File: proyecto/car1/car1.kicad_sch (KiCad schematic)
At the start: 20 parts, among them J1 HC-sr04, J10 Adafruit A, J2 HC-sr04, J3 HC-sr04, J4 USB_C_Receptacle_PowerOnly_6P, J5 SERVO, J6 Adafruit A, J7 Adafruit B, J8 Conn_01x19, J9 Conn_01x19, U1 TB6612FNG

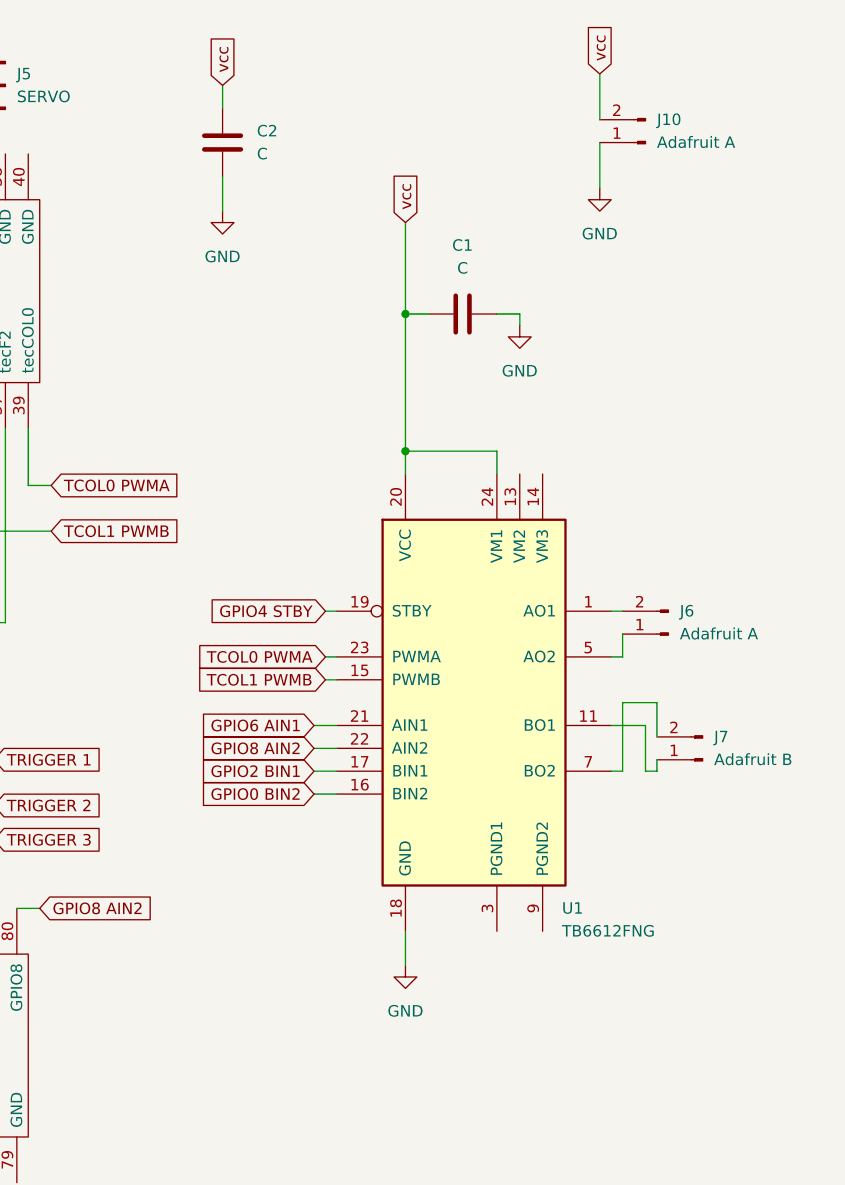
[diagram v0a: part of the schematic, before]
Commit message: se agregaron los componentes
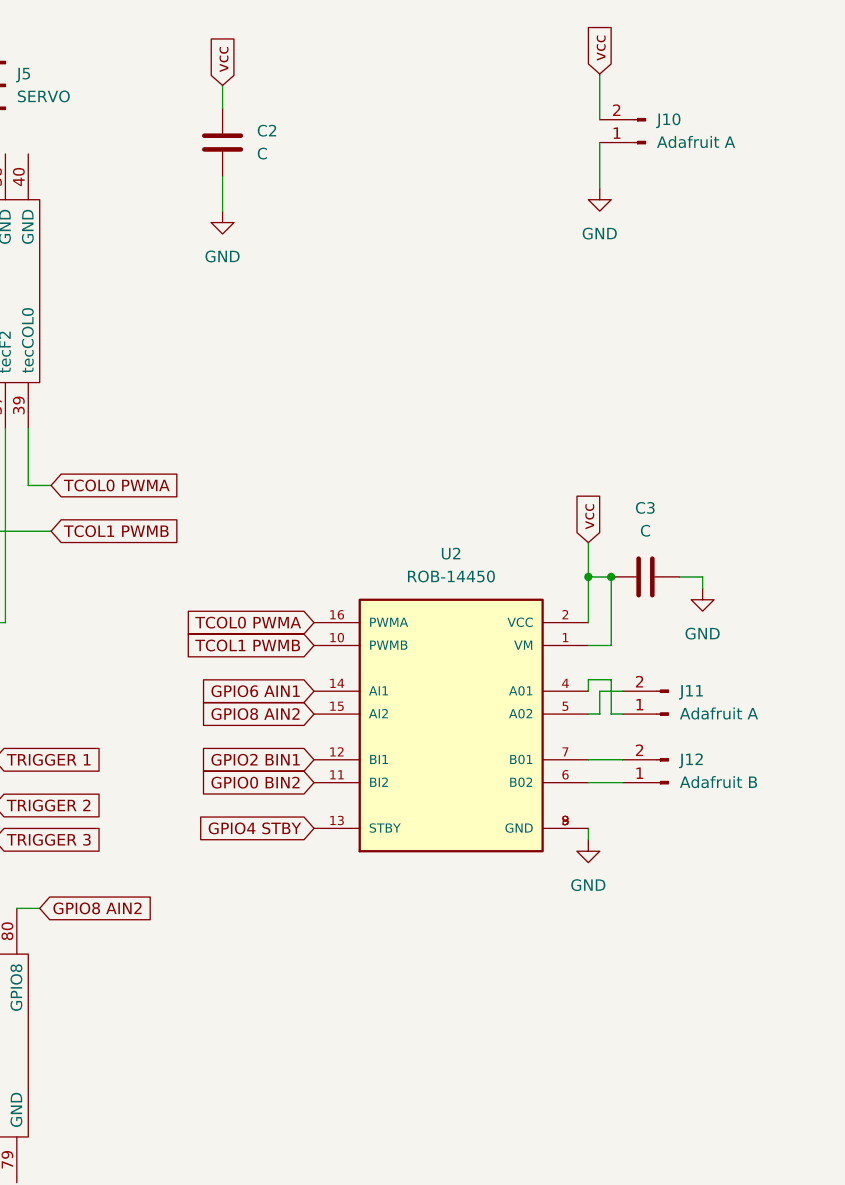
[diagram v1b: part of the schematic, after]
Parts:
- removed C1: C, Capacitor_SMD:C_0201_0603Metric, symbol Device:C
- removed J6: Adafruit A, Connector_Hirose:Hirose_DF63M-2P-3.96DSA_1x02_P3.96mm_Vertical, symbol Connector:Conn_01x02_Pin
- removed J7: Adafruit B, Connector_Hirose:Hirose_DF63M-2P-3.96DSA_1x02_P3.96mm_Vertical, symbol Connector:Conn_01x02_Pin
- removed U1: TB6612FNG, Package_SO:SSOP-24_5.3x8.2mm_P0.65mm, symbol Driver_Motor:TB6612FNG
- added C3: C, Capacitor_SMD:C_0201_0603Metric, symbol Device:C
- added J11: Adafruit A, Connector_Hirose:Hirose_DF63M-2P-3.96DSA_1x02_P3.96mm_Vertical, symbol Connector:Conn_01x02_Pin
- added J12: Adafruit B, Connector_Hirose:Hirose_DF63M-2P-3.96DSA_1x02_P3.96mm_Vertical, symbol Connector:Conn_01x02_Pin
- added U2: ROB-14450, ROB-14450:MODULE_ROB-14450, symbol ROB-14450:ROB-14450
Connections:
- net GND: now also C3.2, U2.3 (GND), U2.8 (GND), U2.9 (GND)
- net GPIO0 BIN2: now also U2.11 (BI2)
- net GPIO2 BIN1: now also U2.12 (BI1)
- net GPIO4 STBY: now also U2.13 (STBY)
- net GPIO6 AIN1: now also U2.14 (AI1)
- net GPIO8 AIN2: now also U2.15 (AI2)
- net TCOL0 PWMA: now also U2.16 (PWMA)
- net TCOL1 PWMB: now also U2.10 (PWMB)
- net vcc: now also C3.1, U2.1 (VM), U2.2 (VCC)
- new net: J11.1 (Pin_1), U2.4 (A01)
- new net: J11.2 (Pin_2), U2.5 (A02)
- new net: J12.1 (Pin_1), U2.6 (B02)
- new net: J12.2 (Pin_2), U2.7 (B01)

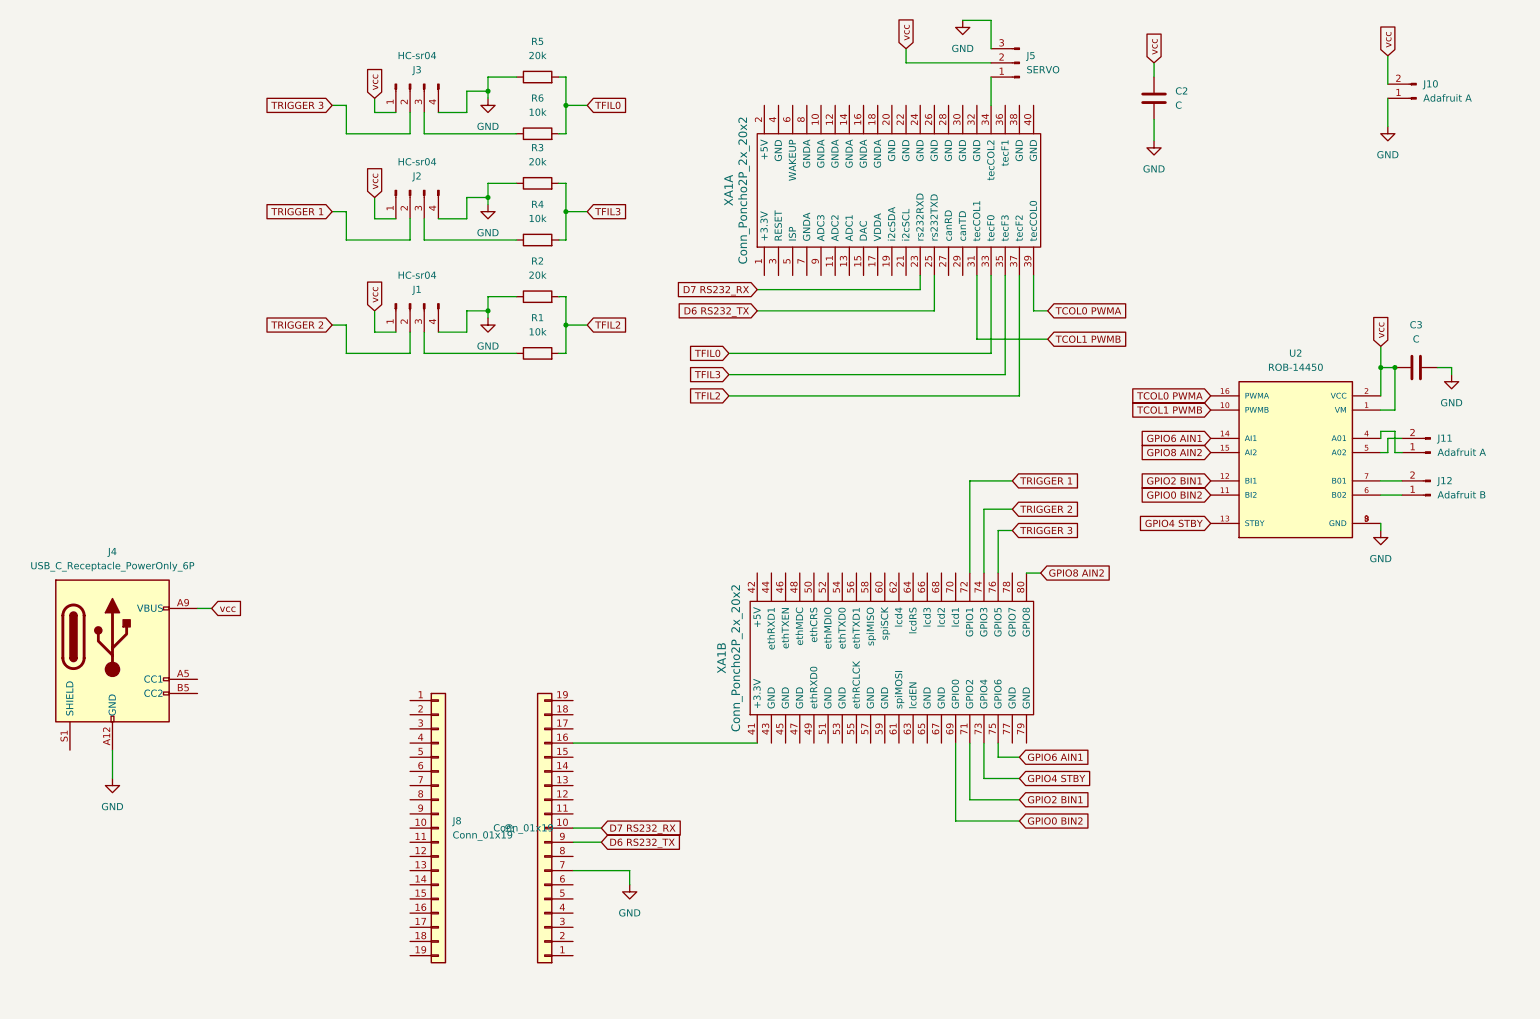
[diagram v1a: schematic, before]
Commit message: se agregaron todos los componentes
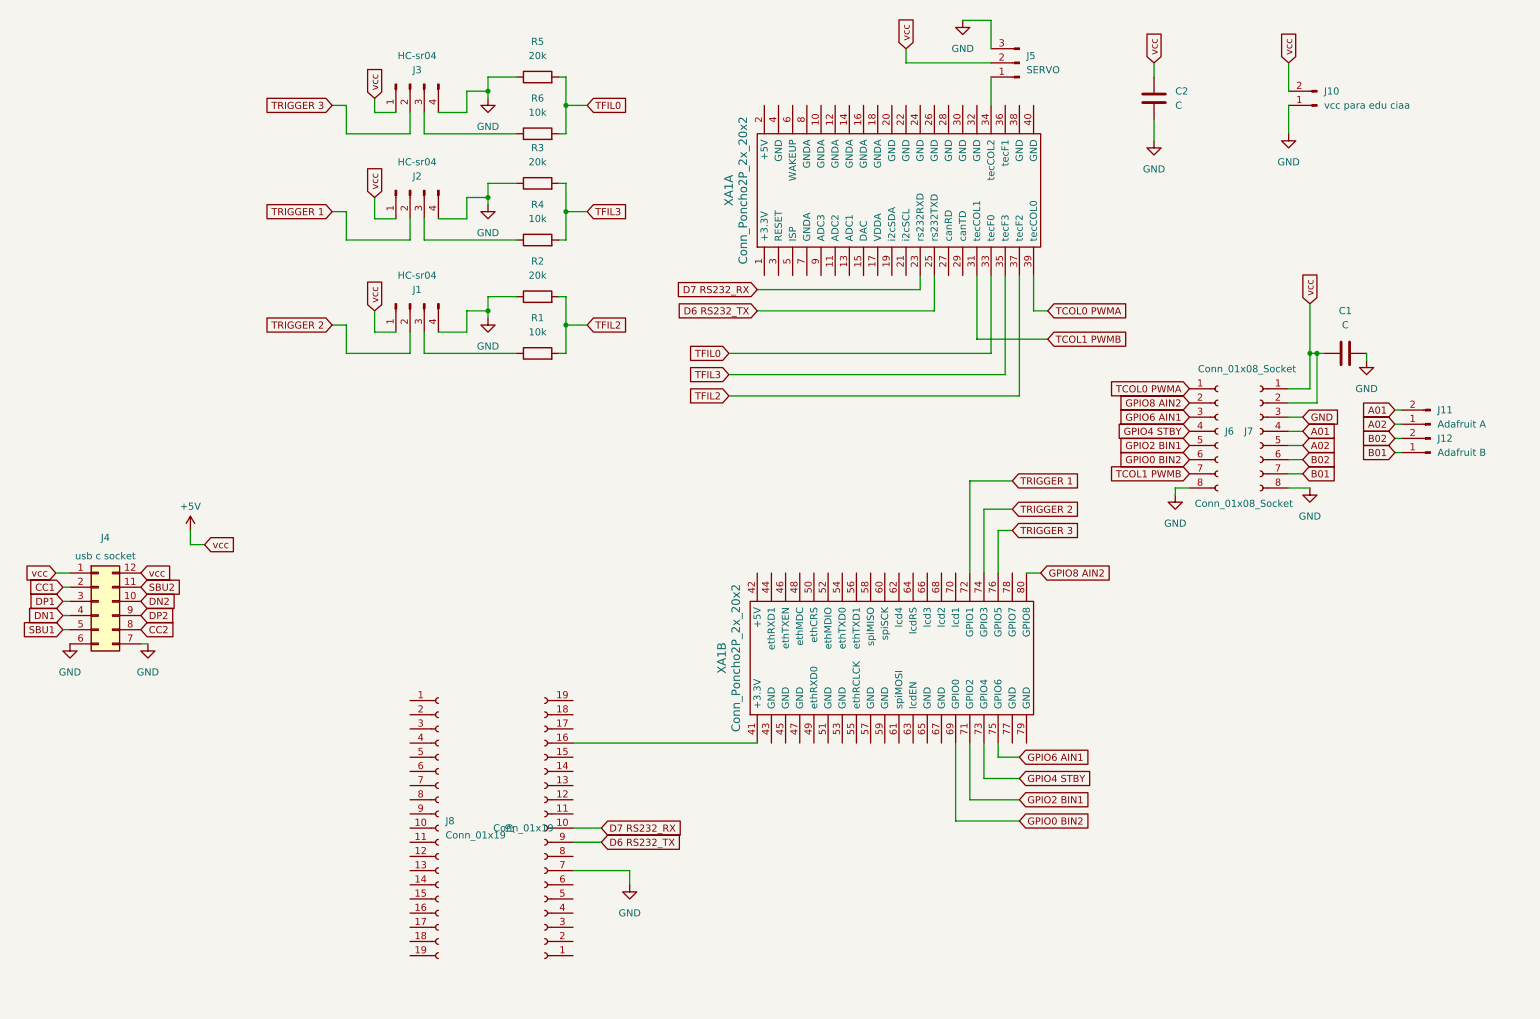
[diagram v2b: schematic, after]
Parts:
- removed C3: C, Capacitor_SMD:C_0201_0603Metric, symbol Device:C
- removed J4: USB_C_Receptacle_PowerOnly_6P, Connector_USB:USB_C_Receptacle_GCT_USB4125-xx-x-0190_6P_TopMnt_Horizontal, symbol Connector:USB_C_Receptacle_PowerOnly_6P
- removed U2: ROB-14450, ROB-14450:MODULE_ROB-14450, symbol ROB-14450:ROB-14450
- added C1: C, Capacitor_SMD:C_1206_3216Metric_Pad1.33x1.80mm_HandSolder, symbol Device:C
- added J4: usb c socket, Connector_PinSocket_2.54mm:PinSocket_2x06_P2.54mm_Vertical, symbol Connector_Generic:Conn_02x06_Counter_Clockwise
- added J6, J7: Conn_01x08_Socket, Connector_PinSocket_2.54mm:PinSocket_1x08_P2.54mm_Vertical, symbol Connector:Conn_01x08_Socket
- C2: footprint Capacitor_SMD:C_0201_0603Metric -> Capacitor_SMD:C_1206_3216Metric_Pad1.33x1.80mm_HandSolder
- J1, J2, J3: footprint Connector_Hirose:Hirose_DF63M-4P-3.96DSA_1x04_P3.96mm_Vertical -> Connector_Molex:Molex_KK-254_AE-6410-04A_1x04_P2.54mm_Vertical
- J10: value Adafruit A -> vcc para edu ciaa; footprint Connector_Hirose:Hirose_DF63M-2P-3.96DSA_1x02_P3.96mm_Vertical -> Connector_Molex:Molex_KK-254_AE-6410-02A_1x02_P2.54mm_Vertical
- J11, J12: footprint Connector_Hirose:Hirose_DF63M-2P-3.96DSA_1x02_P3.96mm_Vertical -> Connector_Molex:Molex_KK-254_AE-6410-02A_1x02_P2.54mm_Vertical
- J5: footprint Connector_JST:JST_XH_B3B-XH-A_1x03_P2.50mm_Vertical -> Connector_Molex:Molex_KK-254_AE-6410-03A_1x03_P2.54mm_Vertical
- J8, J9: footprint Connector_PinHeader_2.54mm:PinHeader_1x19_P2.54mm_Horizontal -> Connector_PinSocket_2.54mm:PinSocket_1x19_P2.54mm_Vertical; symbol Connector_Generic:Conn_01x19 -> Connector:Conn_01x19_Socket
- R1, R2, R3, R4, R5, R6: footprint Resistor_SMD:R_0201_0603Metric -> Resistor_SMD:R_1206_3216Metric_Pad1.30x1.75mm_HandSolder
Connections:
- net GND: now also C1.2, J4.6 (Pin_6), J4.7 (Pin_7), J6.8 (Pin_8), J7.3 (Pin_3), J7.8 (Pin_8)
- net GPIO0 BIN2: now also J6.6 (Pin_6)
- net GPIO2 BIN1: now also J6.5 (Pin_5)
- net GPIO4 STBY: now also J6.4 (Pin_4)
- net GPIO6 AIN1: now also J6.3 (Pin_3)
- net GPIO8 AIN2: now also J6.2 (Pin_2)
- net TCOL0 PWMA: now also J6.1 (Pin_1)
- net TCOL1 PWMB: now also J6.7 (Pin_7)
- net A02: now reaches J11.1 (Pin_1)
- net A02: now also J7.5 (Pin_5)
- net A01: now reaches J11.2 (Pin_2)
- net A01: now also J7.4 (Pin_4)
- net B01: now reaches J12.1 (Pin_1)
- net B01: now also J7.7 (Pin_7)
- net B02: now reaches J12.2 (Pin_2)
- net B02: now also J7.6 (Pin_6)
- net vcc renamed +5V
- net +5V: now also C1.1, J4.1 (Pin_1), J4.12 (Pin_12), J7.1 (Pin_1), J7.2 (Pin_2)
- new net CC1: J4.2 (Pin_2)
- new net CC2: J4.8 (Pin_8)
- new net DN1: J4.4 (Pin_4)
- new net DN2: J4.10 (Pin_10)
- new net DP1: J4.3 (Pin_3)
- new net DP2: J4.9 (Pin_9)
- new net SBU1: J4.5 (Pin_5)
- new net SBU2: J4.11 (Pin_11)
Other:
- moved on the sheet: J10, J11, J12

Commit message: creacion de conexiones
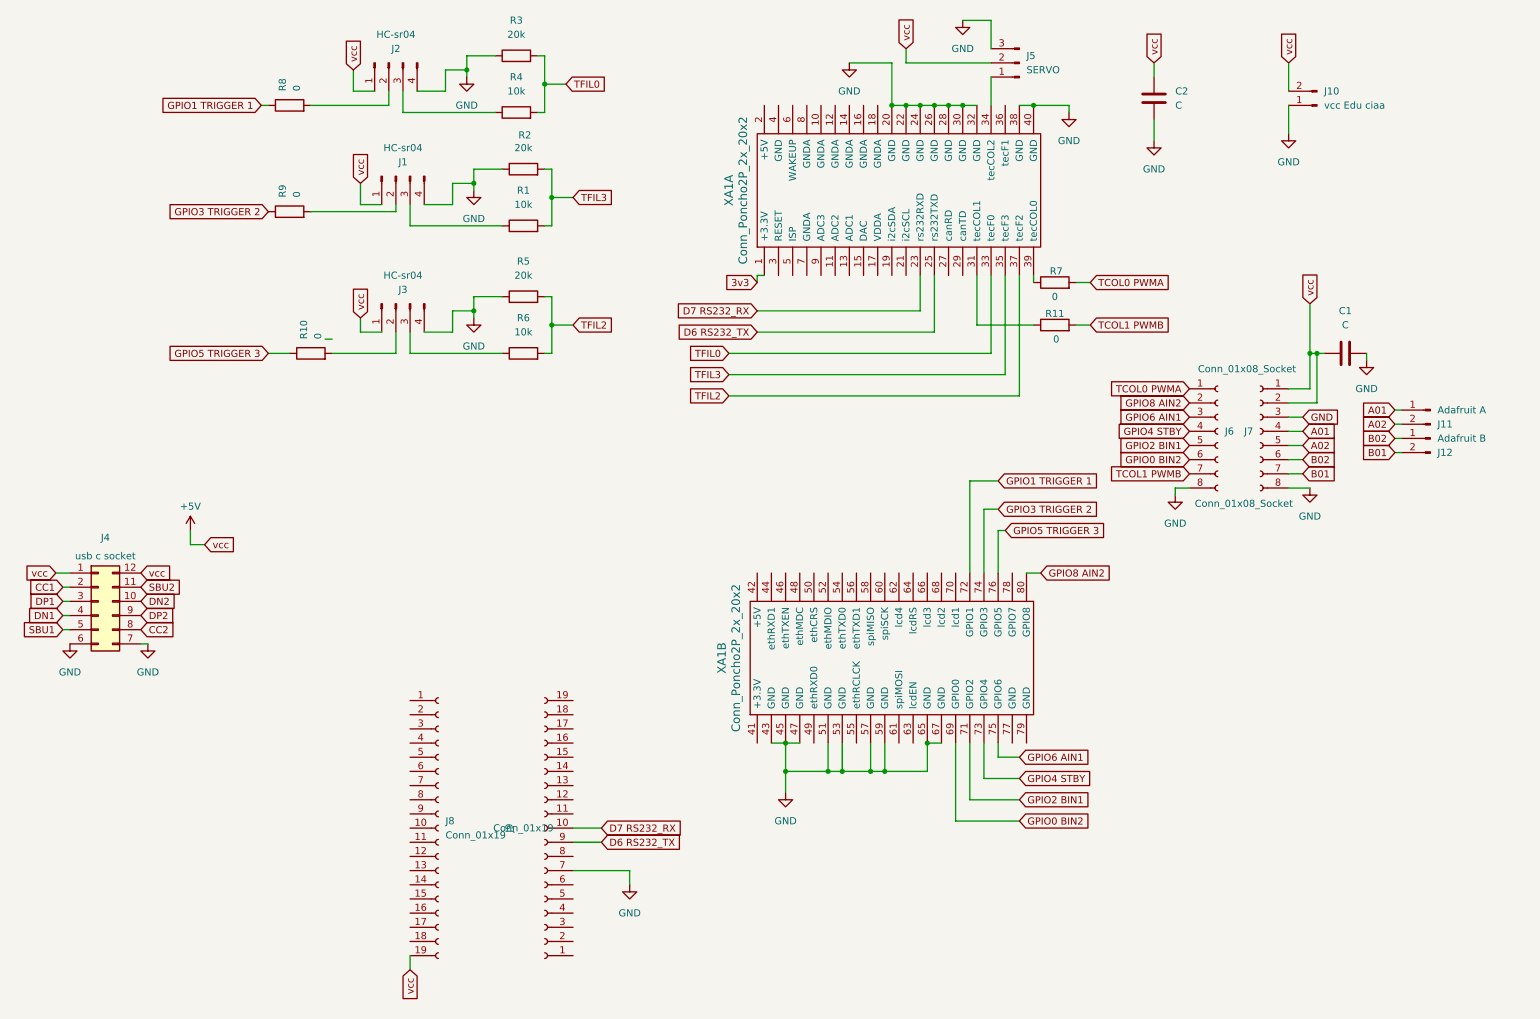
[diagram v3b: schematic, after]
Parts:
- added R10, R11, R7, R8, R9: 0, Resistor_THT:R_Axial_DIN0207_L6.3mm_D2.5mm_P10.16mm_Horizontal, symbol Device:R
- J10: value vcc para edu ciaa -> vcc Edu ciaa
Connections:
- net +5V: now also J8.19 (Pin_19)
- net A01: now also J11.1 (Pin_1); no longer J11.2 (Pin_2)
- net A02: now also J11.2 (Pin_2); no longer J11.1 (Pin_1)
- net B01: now also J12.2 (Pin_2); no longer J12.1 (Pin_1)
- net B02: now also J12.1 (Pin_1); no longer J12.2 (Pin_2)
- net GND: now also XA1.20 (GND), XA1.22 (GND), XA1.24 (GND), XA1.26 (GND), XA1.28 (GND), XA1.30 (GND), XA1.32 (GND), XA1.38 (GND), XA1.40 (GND), XA1.43 (GND), XA1.45 (GND), XA1.47 (GND), XA1.51 (GND), XA1.53 (GND), XA1.57 (GND), XA1.59 (GND), XA1.65 (GND), XA1.67 (GND)
- net TCOL0 PWMA: now also R7.2; no longer XA1.39 (tecCOL0)
- net TCOL1 PWMB: now also R11.2; no longer XA1.31 (tecCOL1)
- net TFIL0: now also R3.2, R4.2; no longer R5.2, R6.2
- net TFIL2: now also R5.2, R6.2; no longer R1.2, R2.2
- net TFIL3: now also R1.2, R2.2; no longer R3.2, R4.2
- net 3v3: now reaches XA1.1 (+3.3V)
- net at XA1.41 (+3.3V): no longer J9.16 (Pin_16)
- net TRIGGER 1: no longer names the net of J2.2 (trigger)
- net TRIGGER 1: now also R8.2; no longer XA1.72 (GPIO1)
- net TRIGGER 2: no longer names the net of J1.2 (trigger)
- net TRIGGER 2: now also R9.2; no longer XA1.74 (GPIO3)
- net TRIGGER 3: no longer names the net of J3.2 (trigger)
- net TRIGGER 3: now also R10.2; no longer XA1.76 (GPIO5)
- new net: R11.1, XA1.31 (tecCOL1)
- new net: R7.1, XA1.39 (tecCOL0)
- new net GPIO1 TRIGGER 1: R8.1, XA1.72 (GPIO1)
- new net GPIO3  TRIGGER 2: R9.1, XA1.74 (GPIO3)
- new net GPIO5 TRIGGER 3: R10.1, XA1.76 (GPIO5)
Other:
- moved on the sheet: J1, J11, J12, J2, J3, R1, R2, R3, R4, R5, R6
